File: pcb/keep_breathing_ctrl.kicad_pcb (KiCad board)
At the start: 4 copper layers, 131 x 112 mm, 167 parts, among them J2 Screw_Terminal, P1 CONN_RASPBERRY, Q1 PN2222, Q2 PN2222, U1 MPL3115A2, U10 PCF8523TK, U11 AQH3213AX, U12 AQH3213AX, U13 HTS221, U14 ICE40UP5K-SG48ITR, U15 GD25Q32CTIGR-Memory_Flash, U16 UCC12040, U17 ISO7762, U18 ZLDO1117G33TA, U2 powerSTEP01, U3 TLP240D, U4 TLP240D, U5 TLP240D, U6 TLP240D, U7 TLP240D, U8 TLP240D, U9 ZLDO1117G33TA, Y1 ABS06-107-32.768KHZ-T

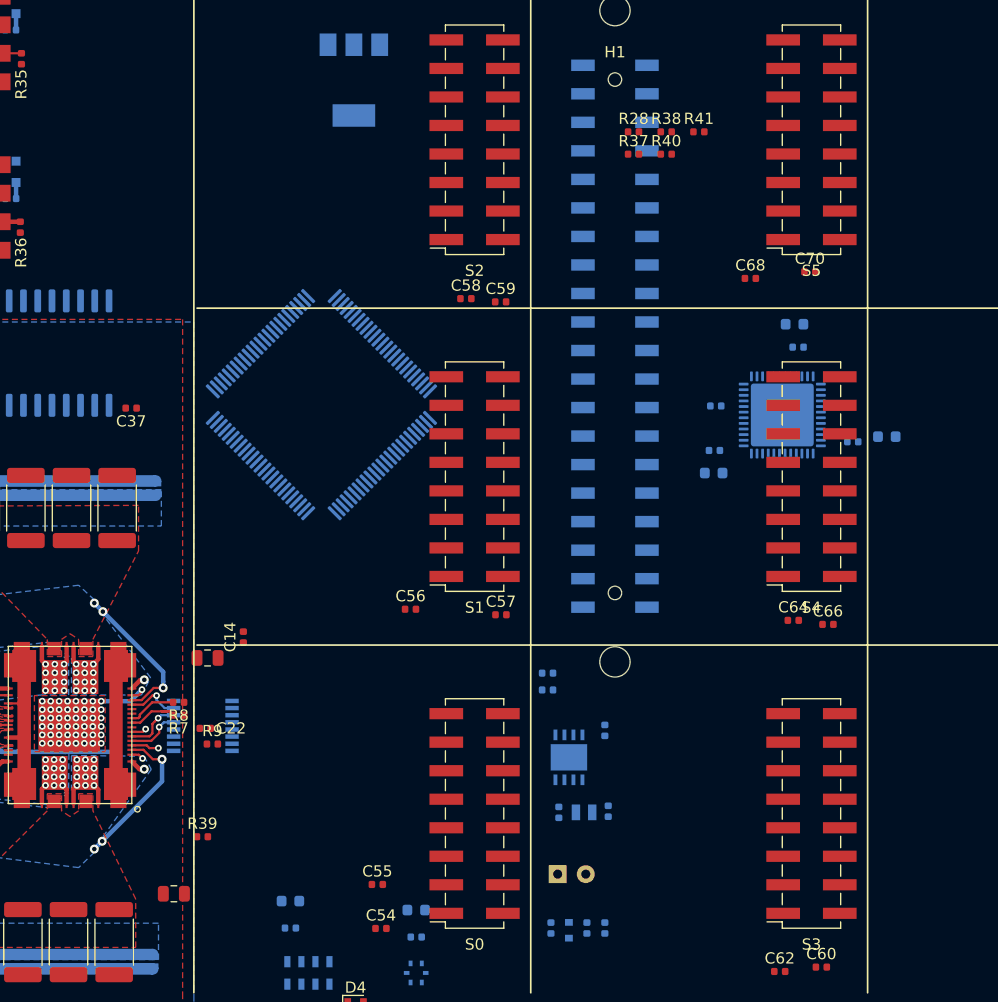
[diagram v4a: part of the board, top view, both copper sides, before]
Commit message: support connectors
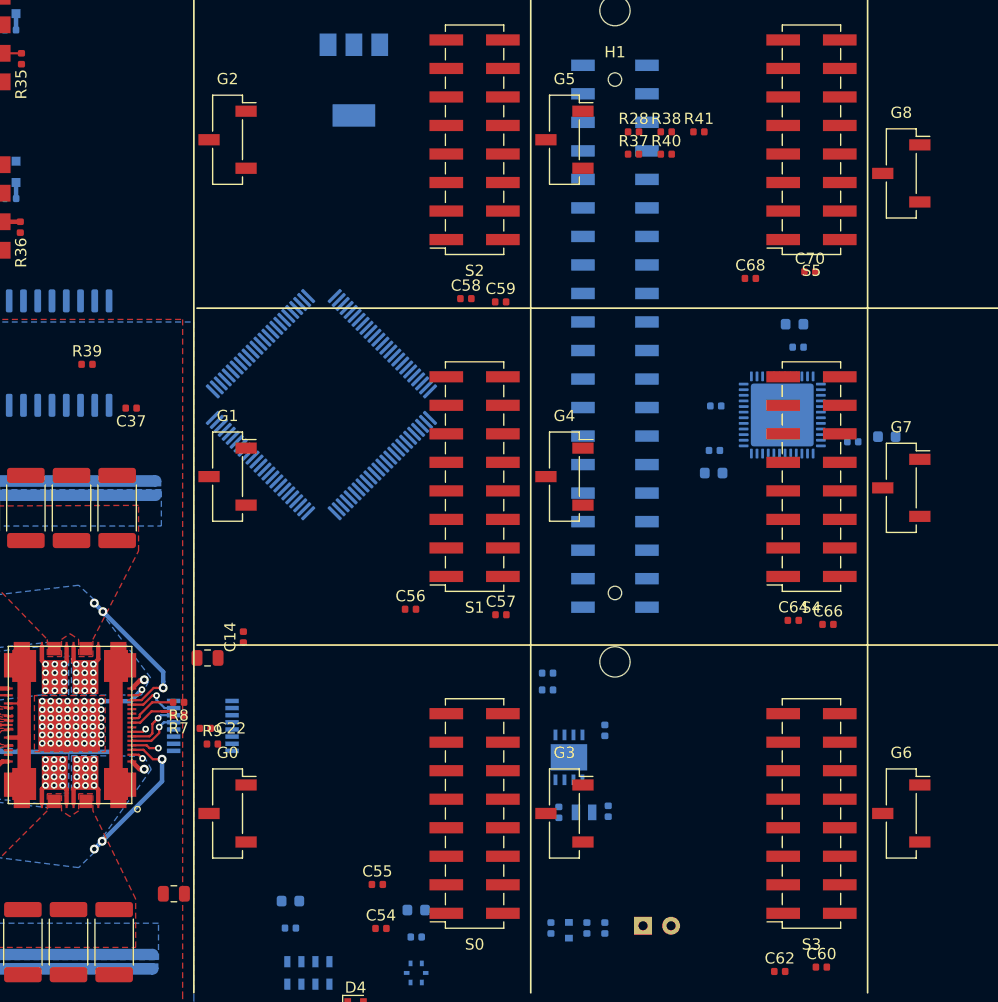
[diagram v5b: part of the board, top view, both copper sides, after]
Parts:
- added G0: Conn_01x03, Connector_PinSocket_2.54mm:PinSocket_1x03_P2.54mm_Vertical_SMD_Pin1Right, F.Cu at (84.0, 125.0)
- added G1: Conn_01x03, Connector_PinSocket_2.54mm:PinSocket_1x03_P2.54mm_Vertical_SMD_Pin1Right, F.Cu at (84.0, 95.0)
- added G2: Conn_01x03, Connector_PinSocket_2.54mm:PinSocket_1x03_P2.54mm_Vertical_SMD_Pin1Right, F.Cu at (84.0, 65.0)
- added G3: Conn_01x03, Connector_PinSocket_2.54mm:PinSocket_1x03_P2.54mm_Vertical_SMD_Pin1Right, F.Cu at (114.0, 125.0)
- added G4: Conn_01x03, Connector_PinSocket_2.54mm:PinSocket_1x03_P2.54mm_Vertical_SMD_Pin1Right, F.Cu at (114.0, 95.0)
- added G5: Conn_01x03, Connector_PinSocket_2.54mm:PinSocket_1x03_P2.54mm_Vertical_SMD_Pin1Right, F.Cu at (114.0, 65.0)
- added G6: Conn_01x03, Connector_PinSocket_2.54mm:PinSocket_1x03_P2.54mm_Vertical_SMD_Pin1Right, F.Cu at (144.0, 125.0)
- added G7: Conn_01x03, Connector_PinSocket_2.54mm:PinSocket_1x03_P2.54mm_Vertical_SMD_Pin1Right, F.Cu at (144.0, 96.0)
- added G8: Conn_01x03, Connector_PinSocket_2.54mm:PinSocket_1x03_P2.54mm_Vertical_SMD_Pin1Right, F.Cu at (144.0, 68.0)
- moved R39 43.3 mm to (71.5, 85.0)
- moved C24 8.88 mm to (121.0, 135.0)

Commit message: replacement
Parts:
- C33, R11, U15: moved to B.Cu
- moved D3 143.1 mm to (41.2, 81.2), turned to 270 degrees
- moved U15 110.8 mm to (134.9, 86.2), turned to 180 degrees
- moved C34 36.1 mm to (65.3, 81.3), turned to 0 degrees
- moved C33 35.8 mm to (67.9, 76.8), turned to 0 degrees
- moved C36 34.0 mm to (65.3, 86.6), turned to 180 degrees
- moved C35 33.3 mm to (61.7, 87.2)
- moved C37 24.8 mm to (80.2, 113.2), turned to 90 degrees
- moved R11 16.5 mm to (44.1, 80.8), turned to 0 degrees
- moved C52 7.60 mm to (128.8, 100.1), turned to 180 degrees
- moved C51 7.51 mm to (141.7, 83.5)
- moved C49 7.22 mm to (141.6, 86.1)
- moved U14 5.76 mm to (135.9, 94.7)
- moved R30 5.44 mm to (129.1, 93.9)
- moved R39 3.75 mm to (68.1, 86.6)
- moved C53 3.69 mm to (128.2, 98.2), turned to 180 degrees
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
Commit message: spi flash placement
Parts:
- C45, R29, R31, R33, R34, R5: moved to B.Cu
- moved R33 162.8 mm to (142.0, 87.8)
- moved R34 157.1 mm to (129.0, 85.0), turned to 180 degrees
- moved R29 139.0 mm to (138.6, 81.3)
- moved C45 131.9 mm to (131.5, 82.0)
- moved R31 129.4 mm to (129.3, 86.9), turned to 180 degrees
- moved R5 114.0 mm to (135.3, 81.2)
- moved D5 103.1 mm to (80.1, 104.8)
- moved C48 68.4 mm to (72.0, 25.7)
- moved R32 68.4 mm to (65.7, 23.9)
- moved C44 59.4 mm to (89.4, 22.2)
- moved C50 59.4 mm to (86.5, 22.2)
- moved C42 59.4 mm to (83.6, 24.2)
- moved C47 59.4 mm to (89.4, 20.2)
- moved C14 10.4 mm to (80.9, 118.7)
- moved R9 7.93 mm to (79.9, 111.4)
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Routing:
- net +5V: track 63.0 -> 52.9 mm
- net 3V3_STM: track 5.03 -> 0.00 mm

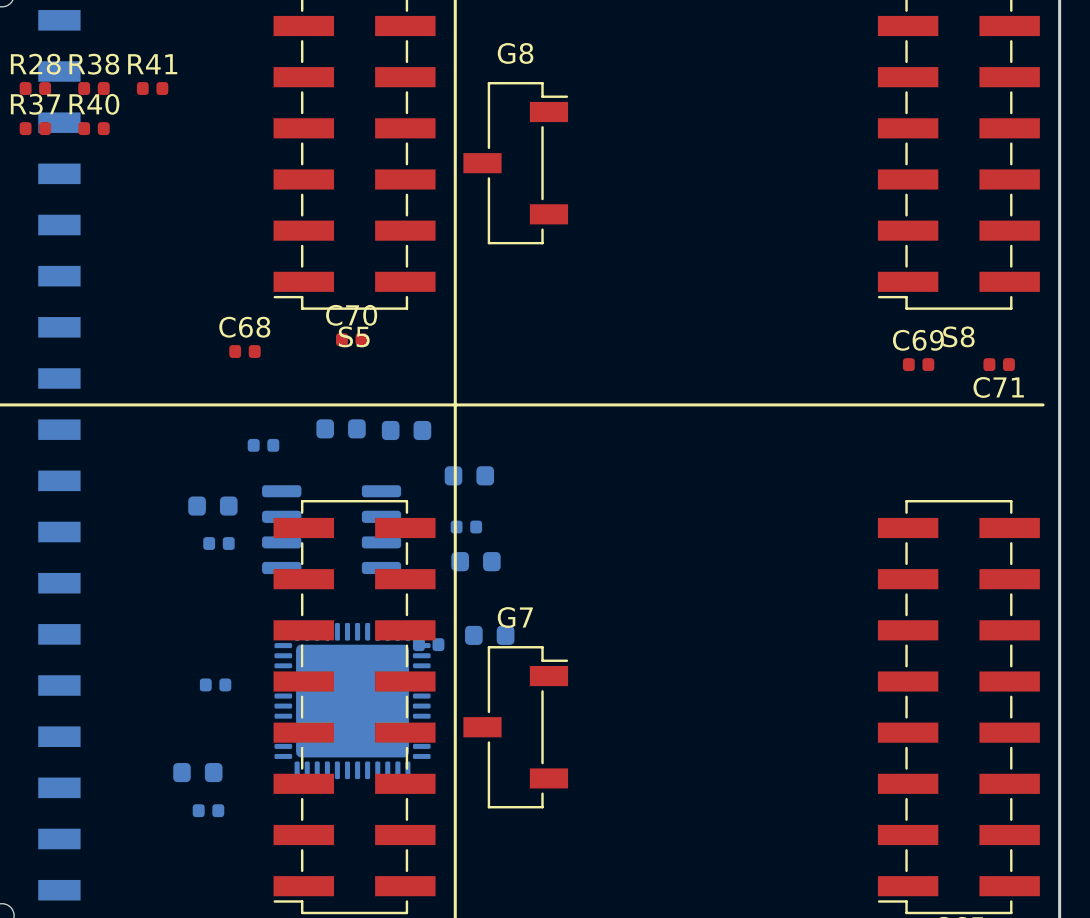
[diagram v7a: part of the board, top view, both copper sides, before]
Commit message: FPGA rotation
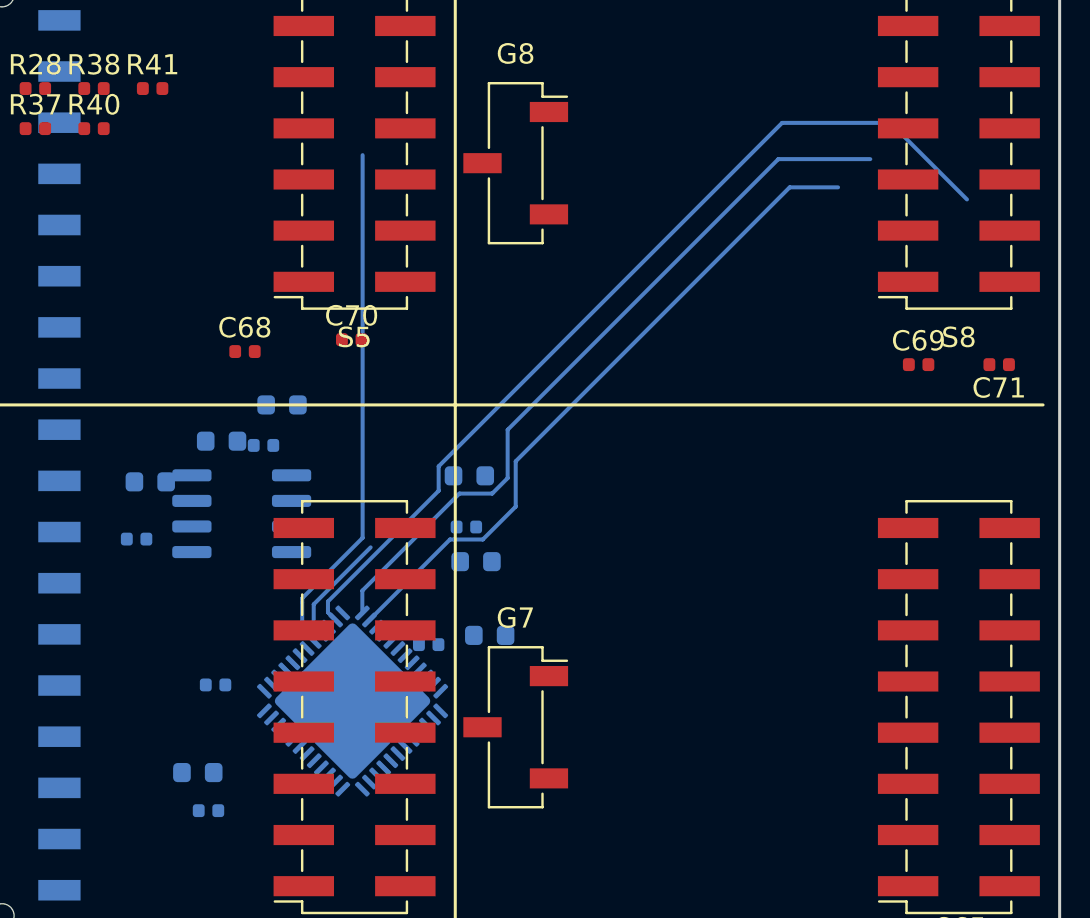
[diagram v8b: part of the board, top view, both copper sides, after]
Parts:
- moved R29 9.20 mm to (129.4, 81.8)
- moved U15 4.53 mm to (130.4, 85.4)
- moved R31 4.10 mm to (125.2, 86.7)
- moved R34 3.33 mm to (125.9, 83.8)
- moved R5 3.16 mm to (132.4, 80.0)
- turned U14 to 45 degrees
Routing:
- net /SensorShields/SPI_CS_8: track 0.00 -> 44.9 mm
- net /SensorShields/I2C_SDA_8: track 0.00 -> 36.6 mm
- net /SensorShields/I2C_CLK_8: track 0.00 -> 33.5 mm
- net /SensorShields/I2C_SDA_5: track 0.00 -> 25.6 mm
- net /SensorShields/SPI_CS_5: track 0.00 -> 5.64 mm
